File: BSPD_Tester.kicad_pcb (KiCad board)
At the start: 2 copper layers, 55.9 x 30.5 mm, 11 parts, among them J1 Conn_02x04_Odd_Even, J2 Conn_01x03, J3 Conn_01x03, J4 Conn_02x04_Odd_Even, J5 Conn_01x02

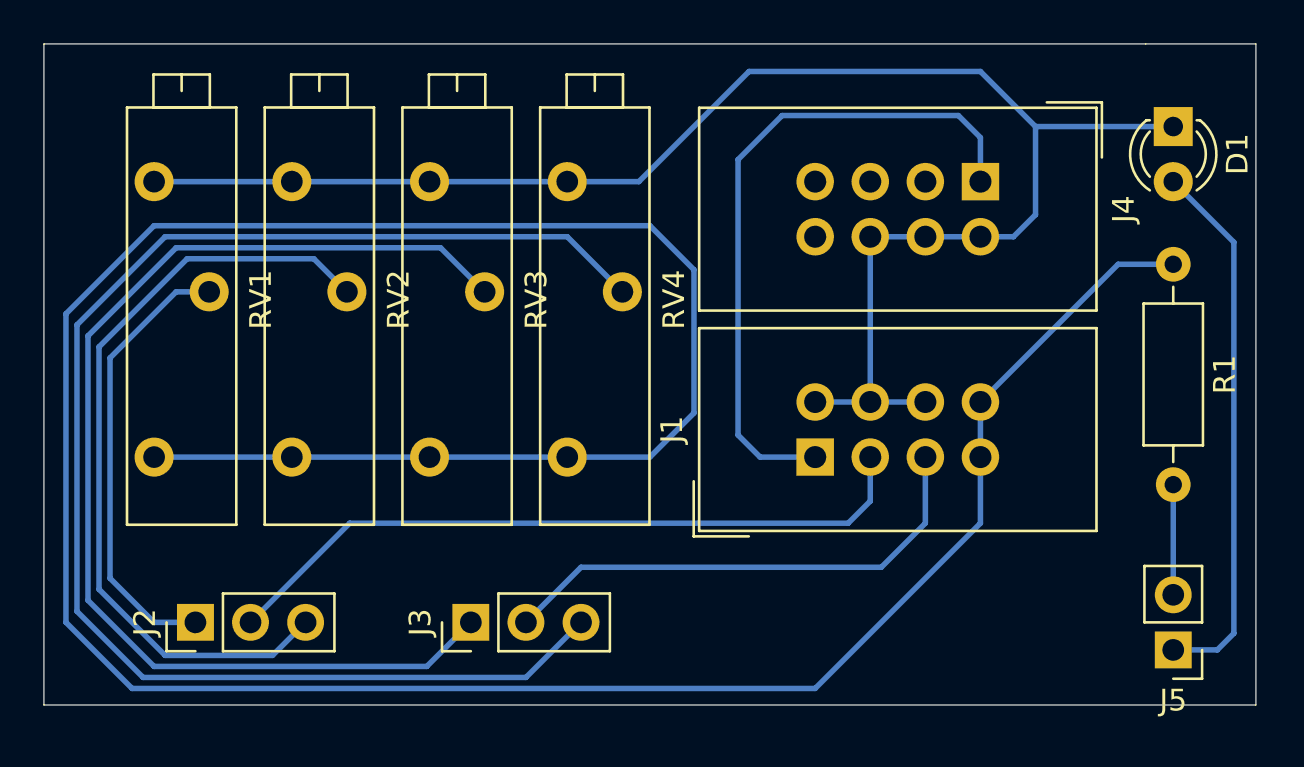
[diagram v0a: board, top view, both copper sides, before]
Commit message: Added better silkscreen for connectors
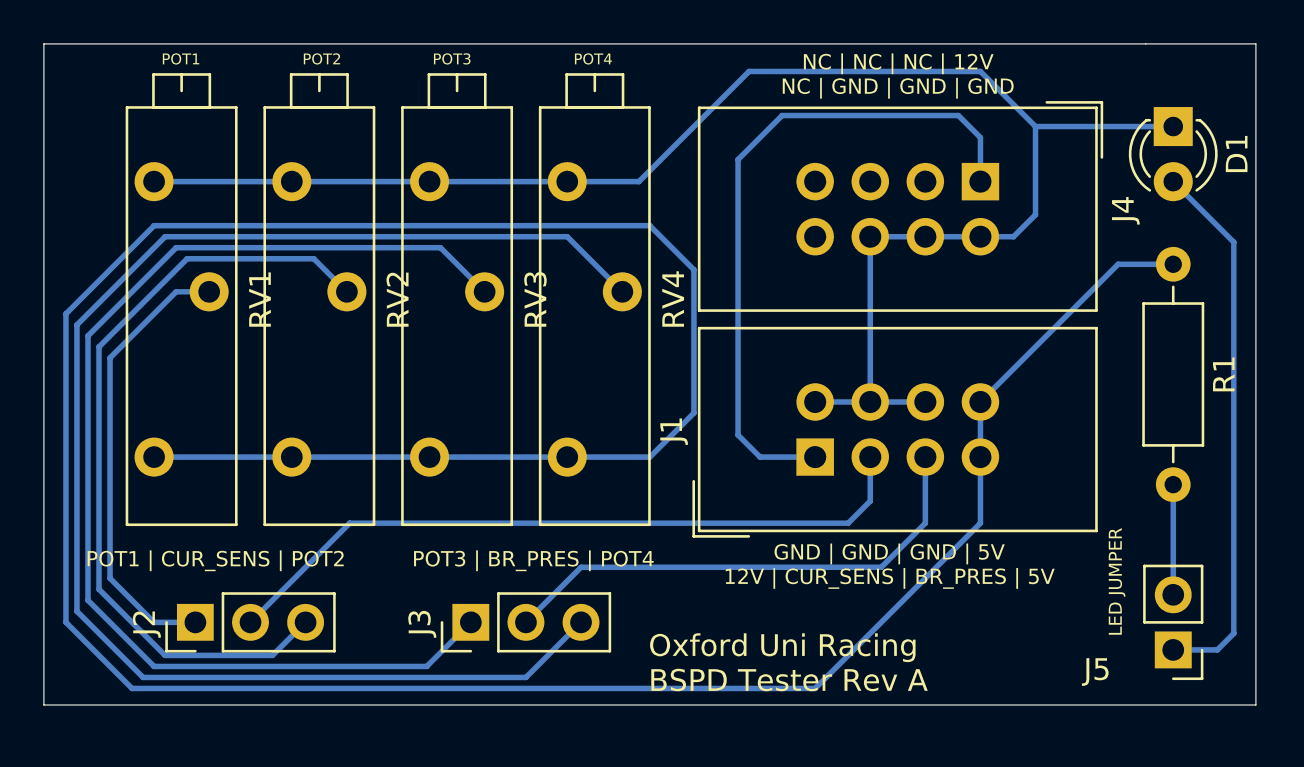
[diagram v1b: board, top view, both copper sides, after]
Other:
- board text added: "GND | GND | GND | 5V 12V | CUR_SENS | BR_PRES | 5V"
- board text added: "LED JUMPER"
- board text added: "NC | NC | NC | 12V NC | GND | GND | GND"
- board text added: "Oxford Uni Racing BSPD Tester Rev A"
- board text added: "POT1"
- board text added: "POT1 | CUR_SENS | POT2"
- board text added: "POT2"
- board text added: "POT3"
- board text added: "POT3 | BR_PRES | POT4"
- board text added: "POT4"
